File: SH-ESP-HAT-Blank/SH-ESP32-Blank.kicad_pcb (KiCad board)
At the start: 4 copper layers, 83 x 55.5 mm, 37 parts, among them J302 GPIO, J303 Conn_01x04, J304 Conn_01x02, J305 Power

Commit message: - Fixed LCSC part number of USB Connector - Change CPU to ESP32-WROOM32E  part (was D)  and fixed LCSC part number - Fixed Name / silkscreen for Blank Tempalte
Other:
- board text added: "TopHat for SH-ESP32 Blank Template"
- board text removed: "Sailor Hat for ESP32 HAT Template"
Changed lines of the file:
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@@
   (gr_line (start 172 90) (end 178 90) (layer B.SilkS) (width 0.12))
   (gr_line (start 172 63) (end 172 90) (layer B.SilkS) (width 0.12))
-  (gr_text "Sailor Hat for ESP32\nHAT Template" (at 116 90) (layer B.SilkS)
+  (gr_text "TopHat for SH-ESP32\nBlank Template" (at 116 90) (layer B.SilkS)
     (effects (font (size 1.4 1.4) (thickness 0.3)) (justify mirror))
   )

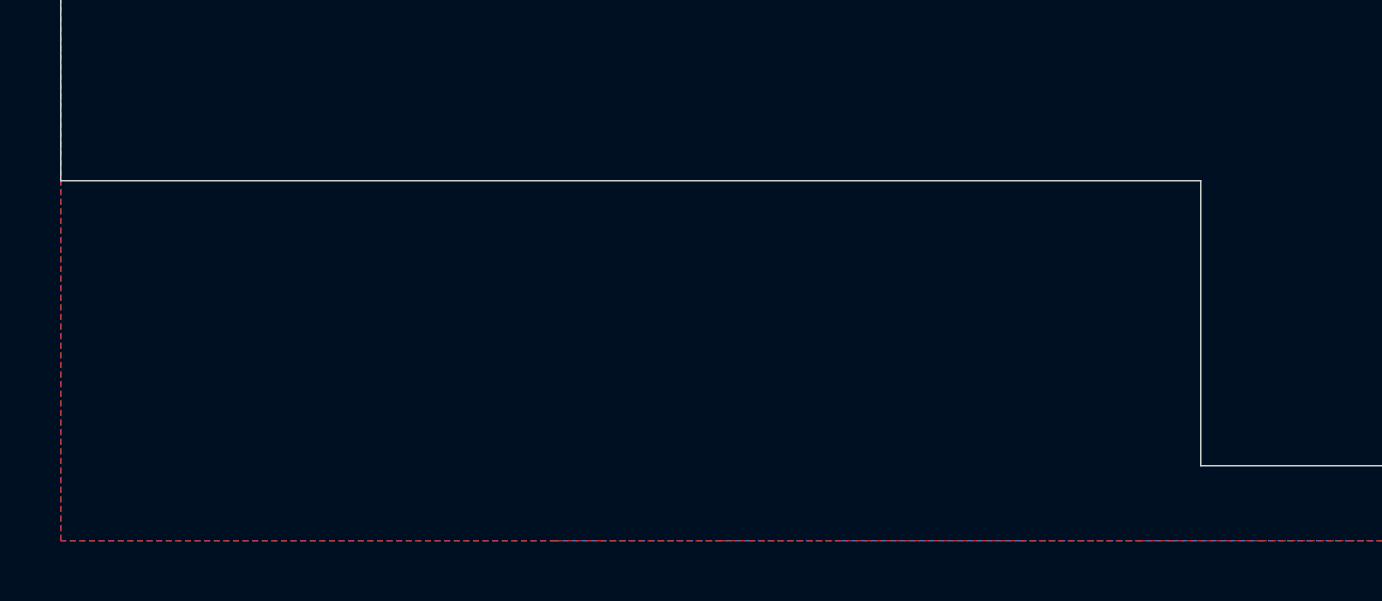
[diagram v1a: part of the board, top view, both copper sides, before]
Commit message: Updated Hat Blank for form factor changes to SH-ESP32 (XH Connectors)
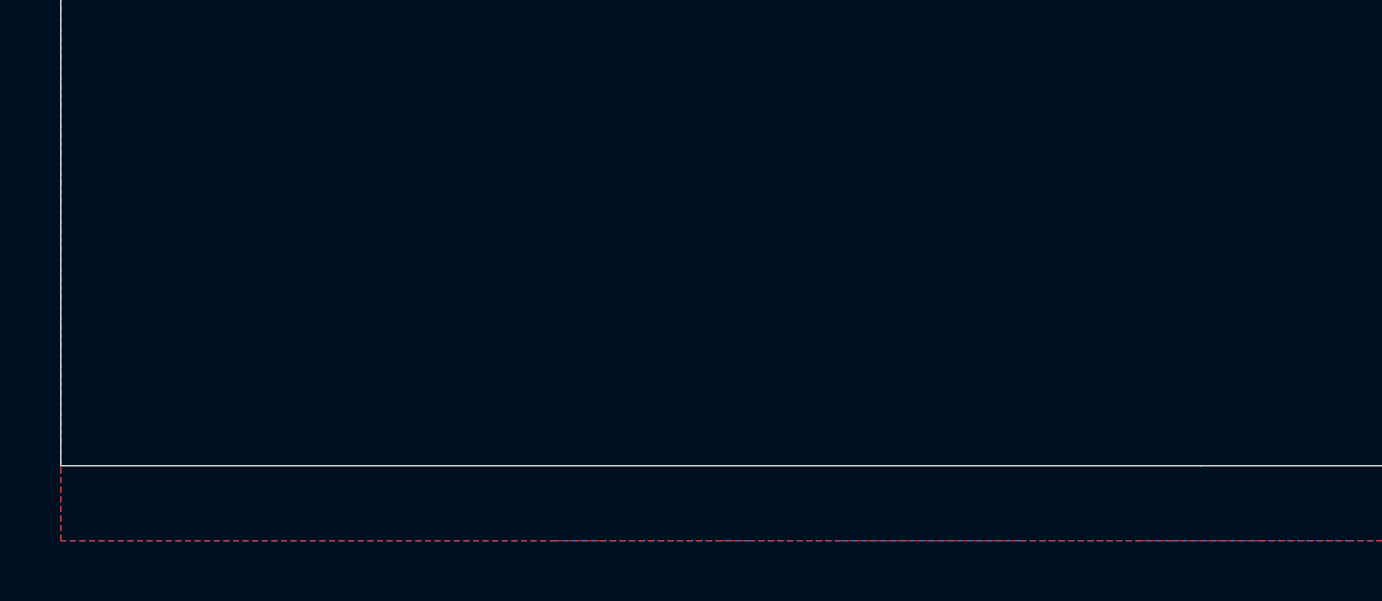
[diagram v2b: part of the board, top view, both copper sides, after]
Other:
- outline, holes or cut-outs redrawn
- board text added: "Revision 0.3.0"
- board text removed: "Revision 0.2.0"
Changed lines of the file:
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@@
       (xy 5.257507 1.511737) (xy 5.40183 1.521577) (xy 5.530535 1.517573)) (layer B.SilkS) (width 0.01))
   )
+  (gr_line (start 89 112.5) (end 89 103) (layer Edge.Cuts) (width 0.05))
+  (gr_line (start 127 112.5) (end 89 112.5) (layer Edge.Cuts) (width 0.05))
   (gr_text +V (at 90.5 96.5) (layer B.SilkS)
     (effects (font (size 0.8 0.8) (thickness 0.16)) (justify mirror))
@@
   (gr_line (start 153 112.5) (end 153 112.5) (layer Edge.Cuts) (width 0.05))
   (gr_line (start 127 112.5) (end 153 112.5) (layer Edge.Cuts) (width 0.05))
-  (gr_line (start 127 112.5) (end 127 103) (layer Edge.Cuts) (width 0.05))
-  (gr_line (start 89 103) (end 127 103) (layer Edge.Cuts) (width 0.05))
   (gr_text "GND & 3.3V" (at 99.568 54.356) (layer Cmts.User)
     (effects (font (size 2 2) (thickness 0.15)))
@@
     (effects (font (size 1.4 1.4) (thickness 0.3)) (justify mirror))
   )
-  (gr_text "Revision 0.2.0" (at 116.5 93.5) (layer B.SilkS)
-    (effects (font (size 1 1) (thickness 0.16)) (justify mirror))
-  )
+  (gr_text "Revision 0.3.0" (at 116.5 93.5) (layer B.SilkS)
+    (effects (font (size 1 1) (thickness 0.16)) (justify mirror))
+  )

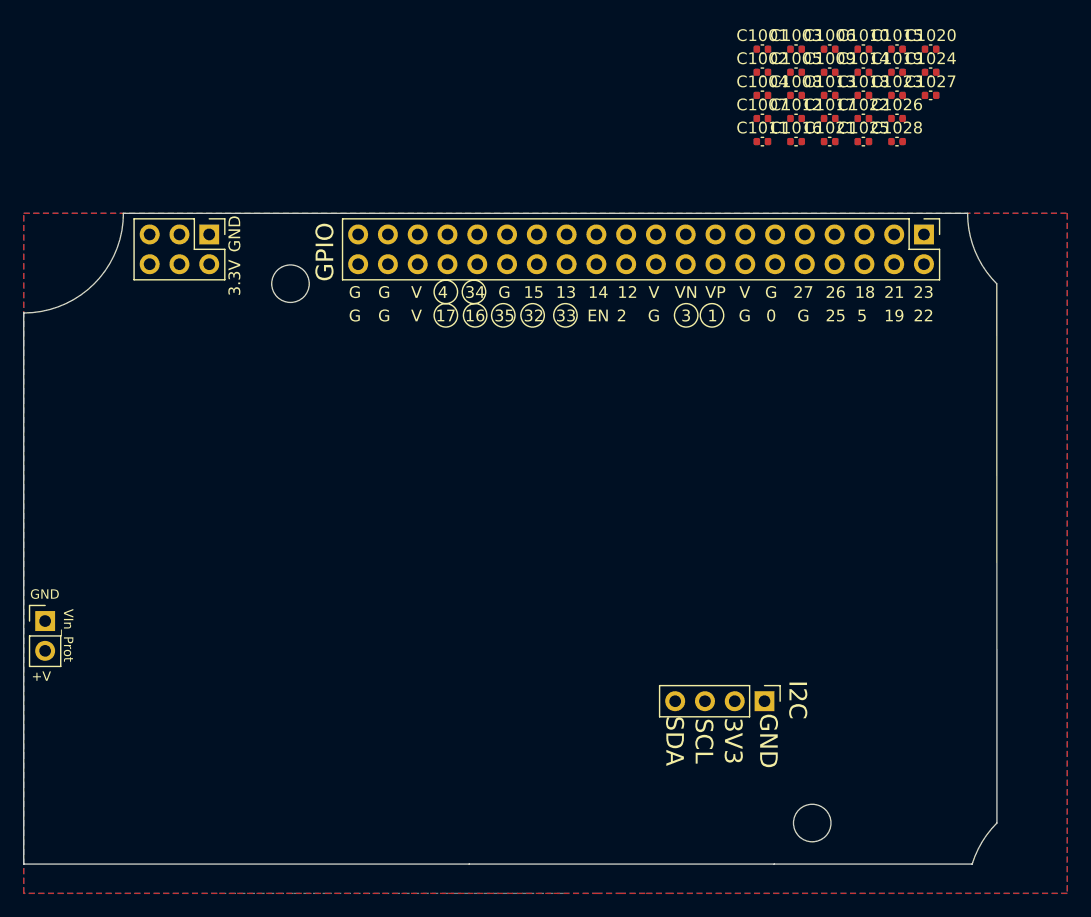
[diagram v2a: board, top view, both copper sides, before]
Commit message: Updated Prot-Blank to R 0.3  matching header pos etc
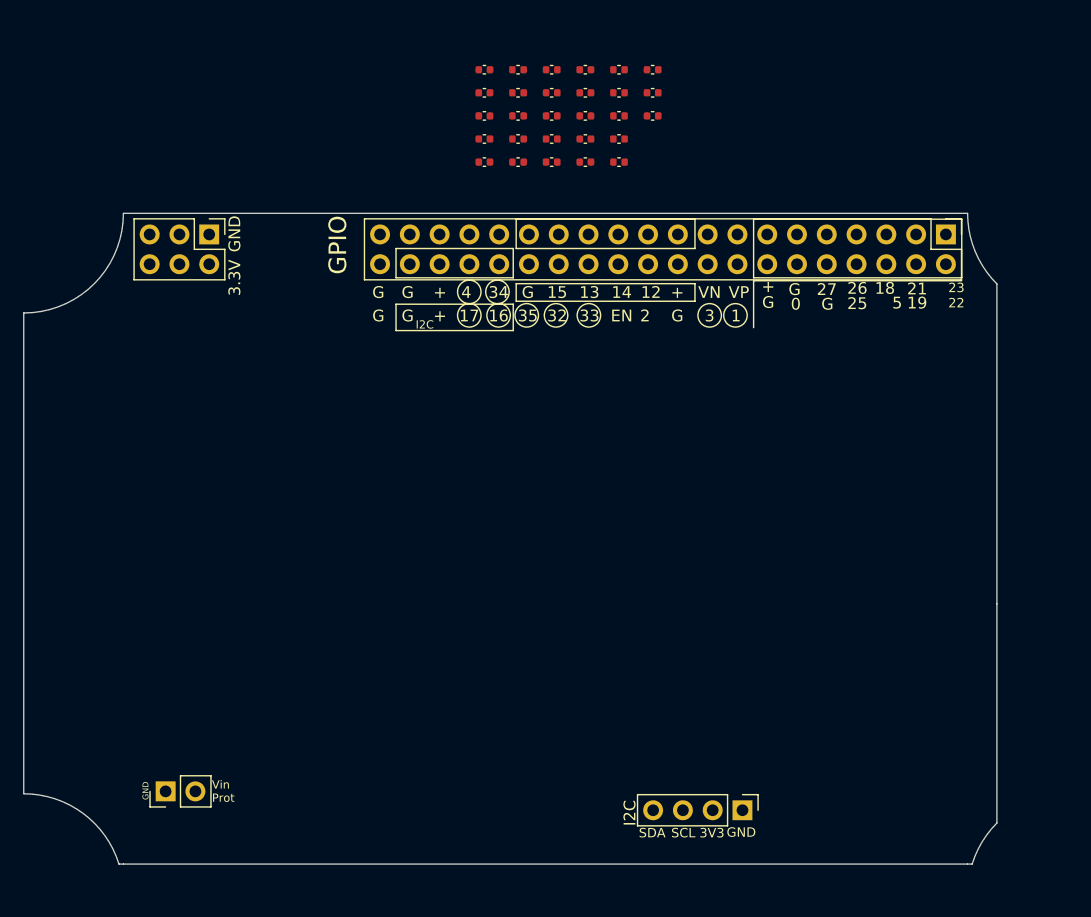
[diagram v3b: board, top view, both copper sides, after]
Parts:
- removed LOGO: LOGO, SH-ESP32:HL-logo-neg
- removed LOGO_CC: LOGO, SH-ESP32:cc-by-sa_silkscreen
- removed OSHW: OSHW-Logo2_14.6x12mm_SilkScreen, Symbol:OSHW-Logo2_14.6x12mm_SilkScreen
- added G***: LOGO, SH-ESP32:Hatlabs-logo-15mm, B.Cu at (78.8, 85.4)
- added G***: LOGO, SH-ESP32:cc-by-sa-10mm, B.Cu at (82.5, 77.9)
- added REF**: OSHW-Logo2_9.8x8mm_SilkScreen, Symbol:OSHW-Logo2_9.8x8mm_SilkScreen, B.Cu at (82.5, 71.4)
- H1001, H1002: footprint SH-ESP32:MountingHole_3.2mm_M3_Unplated -> SH-ESP32:MountingSlot_3.2mm_M3_Unplated
- J303: value Conn_01x04 -> I2C
- moved C1015 36.5 mm to (128.3, 52.6)
- moved C1020 36.5 mm to (131.2, 52.6)
- moved C1006 29.7 mm to (128.3, 46.7)
- moved C1008 26.6 mm to (128.3, 48.7)
- moved C1009 26.6 mm to (131.2, 46.7)
- moved C1010 26.6 mm to (134.0, 44.8)
- moved C1025 26.6 mm to (134.0, 52.6)
- moved C1026 26.6 mm to (136.9, 50.7)
- moved C1027 26.6 mm to (139.8, 48.7)
- moved C1005 26.6 mm to (128.3, 44.8)
- moved C1011 23.7 mm to (128.3, 50.7)
- moved C1012 23.7 mm to (131.2, 48.7)
- moved C1013 23.7 mm to (134.0, 46.7)
- moved C1014 23.7 mm to (136.9, 44.8)
- moved C1016 23.7 mm to (131.2, 50.7)
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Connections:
- J302 pad 1: /IOHeader/IO23 -> (no net)
- J302 pad 12: /IOHeader/IO0 -> (no net)
- J302 pad 15: /IOHeader/SENSOR_VP -> (no net)
- J302 pad 16: /IOHeader/TXD0_C -> (no net)
- J302 pad 17: /IOHeader/SENSOR_VN -> (no net)
- J302 pad 18: /IOHeader/RXD0_C -> (no net)
- J302 pad 2: /IOHeader/IO22 -> (no net)
- J302 pad 21: /IOHeader/IO12 -> (no net)
- J302 pad 22: /IOHeader/IO2 -> (no net)
- J302 pad 23: /IOHeader/IO14 -> (no net)
- J302 pad 24: /IOHeader/EN -> (no net)
- J302 pad 25: /IOHeader/IO13 -> (no net)
- J302 pad 26: /IOHeader/IO33_C -> (no net)
- J302 pad 27: /IOHeader/IO15 -> (no net)
- J302 pad 28: /IOHeader/IO32_C -> (no net)
- J302 pad 3: /IOHeader/IO21 -> (no net)
- J302 pad 30: /IOHeader/IO35_C -> (no net)
- J302 pad 31: /IOHeader/IO34_C -> (no net)
- J302 pad 32: /IOHeader/IO16_C_SDA -> (no net)
- J302 pad 33: /IOHeader/IO4_C -> (no net)
- J302 pad 34: /IOHeader/IO17_C_SCL -> (no net)
- J302 pad 4: /IOHeader/IO19 -> (no net)
- J302 pad 5: /IOHeader/IO18 -> (no net)
- J302 pad 6: /IOHeader/IO5 -> (no net)
- J302 pad 7: /IOHeader/IO26 -> (no net)
- J302 pad 8: /IOHeader/IO25 -> (no net)
- J302 pad 9: /IOHeader/IO27 -> (no net)
- J303 pad 3: /IOHeader/SCL -> (no net)
- J303 pad 4: /IOHeader/SDA -> (no net)
- J304 pad 2: /IOHeader/Vin_protected -> (no net)
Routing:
- removed copper zone on B.Cu, net GND
- removed copper zone on F.Cu, net GND
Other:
- outline, holes or cut-outs redrawn
- board text added: "+"
- board text added: "1-Wire"
- board text added: "CAN bus"
- board text added: "Opto- coupled GPIO"
- board text added: "Power"
- board text added: "Sailor Hat with ESP32"
- board text added: "USB"
- board text added: "USB impedance controlled traces designed for the JLC7628 stackup"
- board text added: "User I/O Header"
- board text added: "VIn Prot"
- board text added: "Vin Prot"
- board text added: "Vin_Prot for Hat Daughter board"
- board text added: "https://github.com/hatlabs/SH-ESP32-hardware/"
- board text removed: "+V"
- board text removed: "JLCJLCJLCJLC"
- board text removed: "TopHat for SH-ESP32 Blank Template"
- board text removed: "V"
- board text removed: "VIn_Prot"

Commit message: Groundpllane on Hat-Proto & moved KeepOut on Blank to user Cmts
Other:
- board text removed: "1-Wire"
- board text removed: "CAN bus"
- board text removed: "Opto- coupled GPIO"
- board text removed: "Power"
- board text removed: "USB"
- board text removed: "USB impedance controlled traces designed for the JLC7628 stackup"
- board text removed: "User I/O Header"
- board text removed: "Vin_Prot for Hat Daughter board"
